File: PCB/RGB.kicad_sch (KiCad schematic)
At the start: 70 parts, among them J9 RGB_EX

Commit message: Added large caps to output of TPS2557. Updated STEP file and file data.
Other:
- company: (none) -> Created by Ariamelon (https://github.com/Ariamelon/Honeydew/)
- title: Honeydew unsplit ergonomic keyboard -> Honeydew unified split ergonomic keyboard
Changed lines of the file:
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@@
   (paper "A4")
   (title_block
-    (title "Honeydew unsplit ergonomic keyboard")
-    (date "2023-04-03")
+    (title "Honeydew unified split ergonomic keyboard")
+    (date "2023-04-08")
     (rev "V2.0")
+    (company "Created by Ariamelon (https://github.com/Ariamelon/Honeydew/)")
     (comment 1 "All capacitors 50V unless otherwise specified.")
+    (comment 2 "Licensed under CC BY 4.0.")
   )
   (junction (at 234.95 60.96) (diameter 0) (color 0 0 0 0)

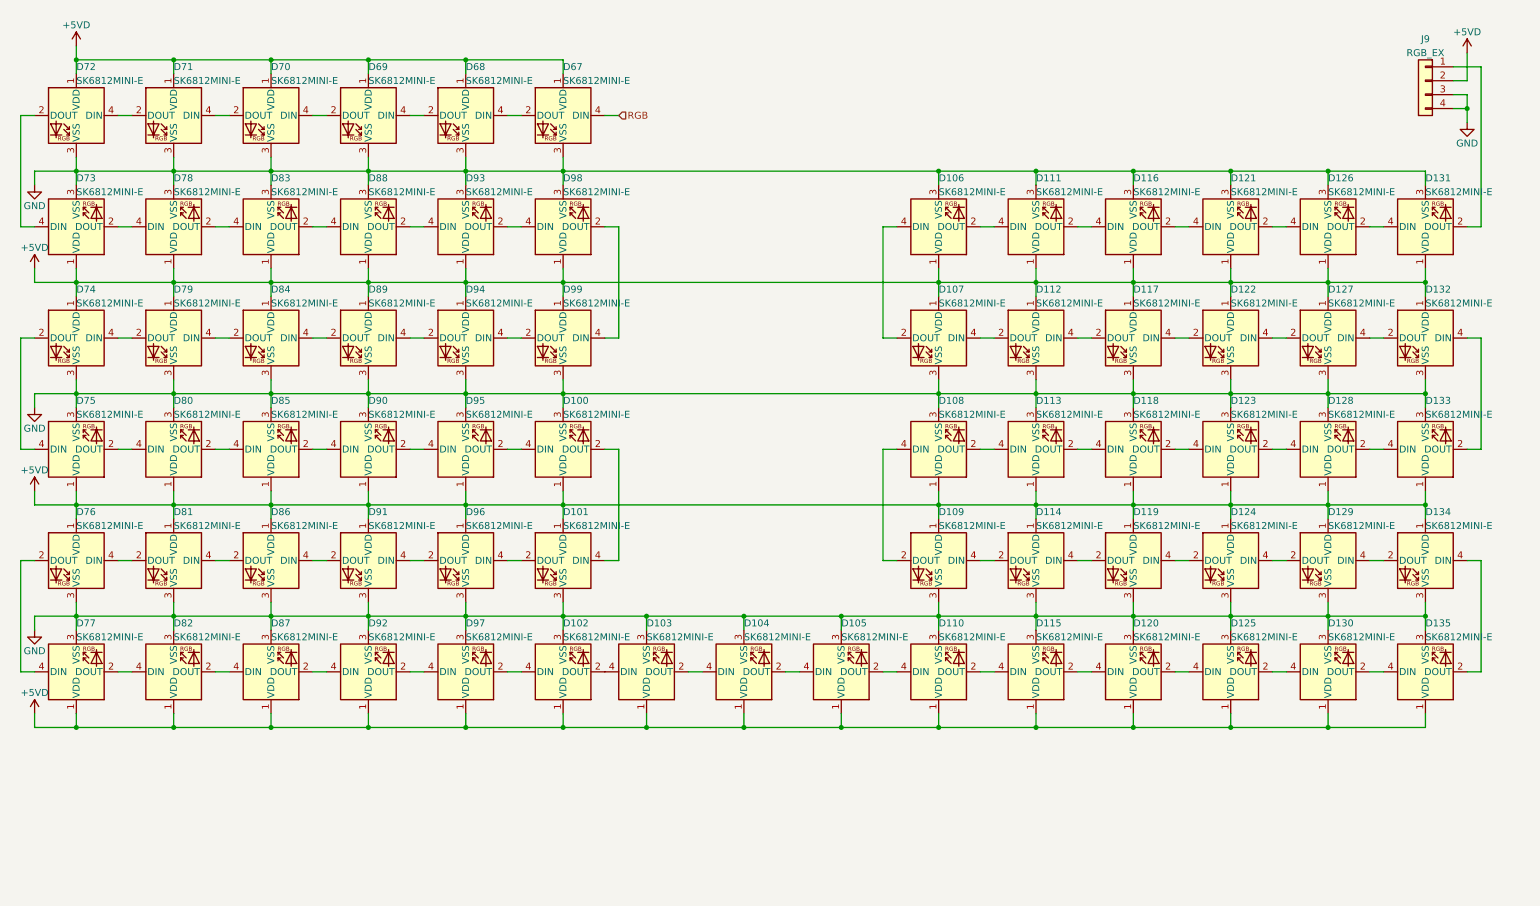
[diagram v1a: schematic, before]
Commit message: Shrunk size of PCB.
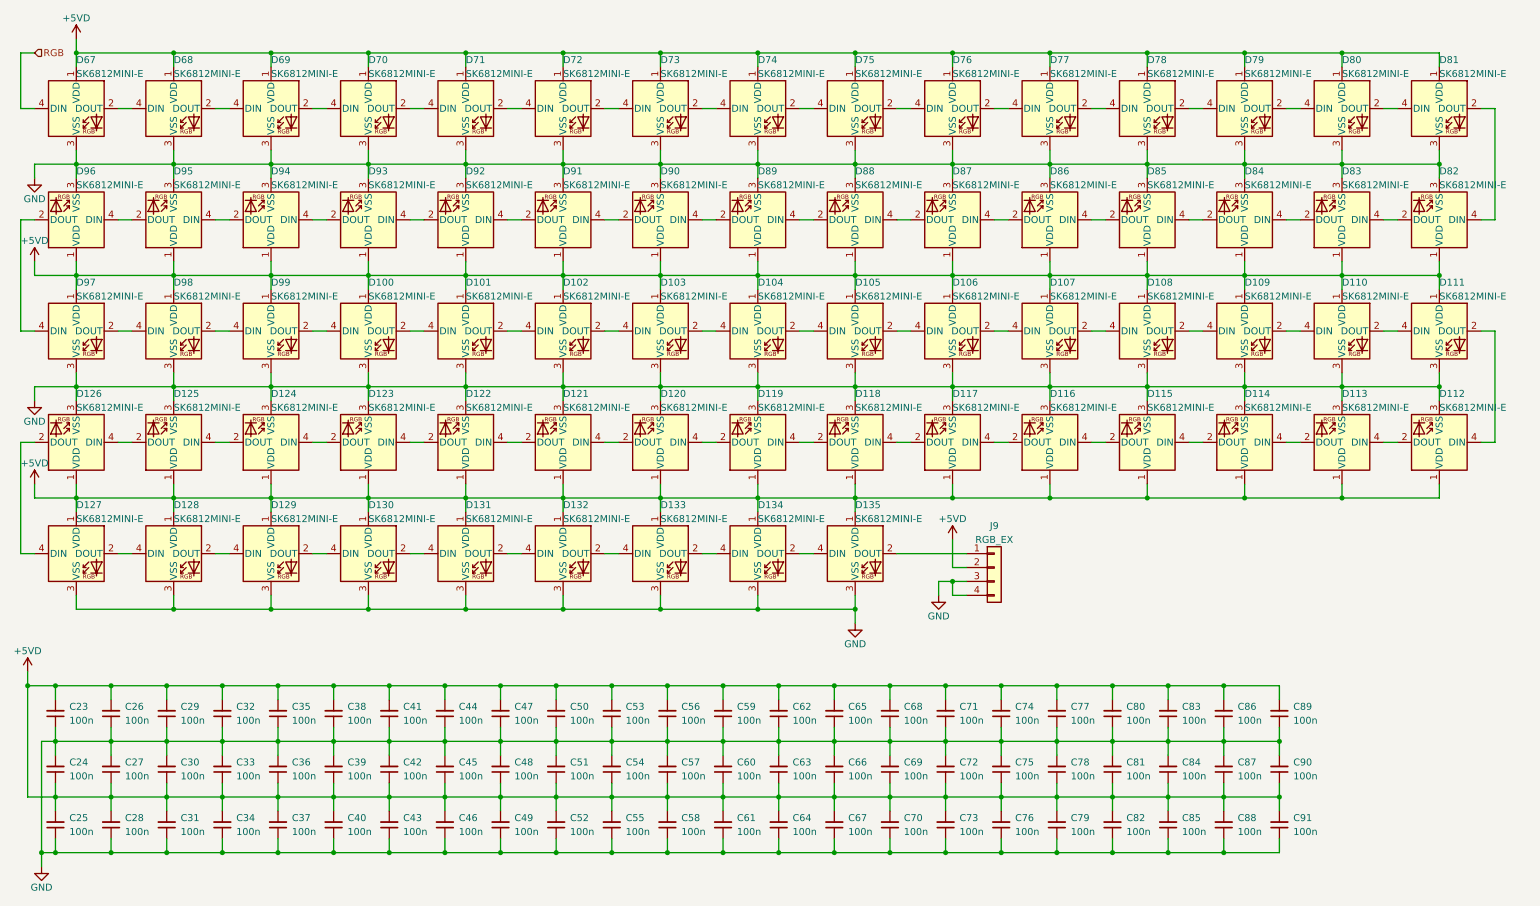
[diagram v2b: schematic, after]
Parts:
- added C23, C24, C25, C26, C27, C28, C29, C30, C31, C32, C33, C34, C35, C36, C37, C38, C39, C40, C41, C42, C43, C44, C45, C46, C47, C48, C49, C50, C51, C52, C53, C54, C55, C56, C57, C58, C59, C60, C61, C62, C63, C64, C65, C66, C67, C68, C69, C70, C71, C72, C73, C74, C75, C76, C77, C78, C79, C80, C81, C82, C83, C84, C85, C86, C87, C88, C89, C90, C91: 100n, Honeydew:C_0402_1005Metric, symbol Device:C_Small
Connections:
- net +5VD: now also C23.2, C24.1, C25.2, C26.2, C27.1, C28.2, C29.2, C30.1, C31.2, C32.2, C33.1, C34.2, C35.2, C36.1, C37.2, C38.2, C39.1, C40.2, C41.2, C42.1, C43.2, C44.2, C45.1, C46.2, C47.2, C48.1, C49.2, C50.2, C51.1, C52.2, C53.2, C54.1, C55.2, C56.2, C57.1, C58.2, C59.2, C60.1, C61.2, C62.2, C63.1, C64.2, C65.2, C66.1, C67.2, C68.2, C69.1, C70.2, C71.2, C72.1, C73.2, C74.2, C75.1, C76.2, C77.2, C78.1, C79.2, C80.2, C81.1, C82.2, C83.2, C84.1, C85.2, C86.2, C87.1, C88.2, C89.2, C90.1, C91.2
- net GND: now also C23.1, C24.2, C25.1, C26.1, C27.2, C28.1, C29.1, C30.2, C31.1, C32.1, C33.2, C34.1, C35.1, C36.2, C37.1, C38.1, C39.2, C40.1, C41.1, C42.2, C43.1, C44.1, C45.2, C46.1, C47.1, C48.2, C49.1, C50.1, C51.2, C52.1, C53.1, C54.2, C55.1, C56.1, C57.2, C58.1, C59.1, C60.2, C61.1, C62.1, C63.2, C64.1, C65.1, C66.2, C67.1, C68.1, C69.2, C70.1, C71.1, C72.2, C73.1, C74.1, C75.2, C76.1, C77.1, C78.2, C79.1, C80.1, C81.2, C82.1, C83.1, C84.2, C85.1, C86.1, C87.2, C88.1, C89.1, C90.2, C91.1
- net at D89.4 (DIN): now also D88.2 (DOUT); no longer D94.2 (DOUT)
- net at D94.4 (DIN): now also D93.2 (DOUT); no longer D99.2 (DOUT)
- net at D110.2 (DOUT): now also D111.4 (DIN); no longer D115.4 (DIN)
- net at D105.2 (DOUT): now also D106.4 (DIN); no longer D110.4 (DIN)
- net at D132.4 (DIN): now also D131.2 (DOUT); no longer D133.2 (DOUT)
- net at D128.2 (DOUT): now also D129.4 (DIN); no longer D133.4 (DIN)
- net at D74.4 (DIN): now also D73.2 (DOUT); no longer D79.2 (DOUT)
- net at D79.4 (DIN): now also D78.2 (DOUT); no longer D84.2 (DOUT)
- net at D89.2 (DOUT): now also D90.4 (DIN); no longer D84.4 (DIN)
- net at D107.2 (DOUT): now also D108.4 (DIN); no longer D106.4 (DIN)
- net at D107.4 (DIN): now also D106.2 (DOUT); no longer D112.2 (DOUT)
- net at D81.2 (DOUT): now also D82.4 (DIN); no longer D76.4 (DIN)
- net at D86.2 (DOUT): now also D87.4 (DIN); no longer D81.4 (DIN)
- net at D130.2 (DOUT): now also D131.4 (DIN); no longer D135.4 (DIN)
- net at D125.2 (DOUT): now also D126.4 (DIN); no longer D130.4 (DIN)
- net at D83.4 (DIN): now also D82.2 (DOUT); no longer D78.2 (DOUT)
- net at D78.4 (DIN): now also D77.2 (DOUT); no longer D73.2 (DOUT)
- net at D88.4 (DIN): now also D87.2 (DOUT); no longer D83.2 (DOUT)
- net at D98.4 (DIN): now also D97.2 (DOUT); no longer D93.2 (DOUT)
- net at D92.2 (DOUT): now also D93.4 (DIN); no longer D97.4 (DIN)
- net at D92.4 (DIN): now also D91.2 (DOUT); no longer D87.2 (DOUT)
- net at D111.2 (DOUT): now also D112.4 (DIN); no longer D116.4 (DIN)
- net at D115.2 (DOUT): now also D116.4 (DIN); no longer D120.4 (DIN)
- net at D125.4 (DIN): now also D124.2 (DOUT); no longer D120.2 (DOUT)
- net at D126.2 (DOUT): now also D127.4 (DIN); no longer D131.4 (DIN)
- net at D121.2 (DOUT): now also D122.4 (DIN); no longer D126.4 (DIN)
- net at D102.4 (DIN): now also D101.2 (DOUT); no longer D97.2 (DOUT)
- net at D86.4 (DIN): now also D85.2 (DOUT); no longer D91.2 (DOUT)
- net at D116.2 (DOUT): now also D117.4 (DIN); no longer D121.4 (DIN)
- net at D100.4 (DIN): now also D99.2 (DOUT); no longer D95.2 (DOUT)
- net at D127.2 (DOUT): now also D128.4 (DIN); no longer D122.4 (DIN)
- net at D132.2 (DOUT): now also D133.4 (DIN); no longer D127.4 (DIN)
- net at D109.2 (DOUT): now also D110.4 (DIN); no longer D108.4 (DIN)
- net at D114.2 (DOUT): now also D115.4 (DIN); no longer D109.4 (DIN)
- net at D95.4 (DIN): now also D94.2 (DOUT); no longer D90.2 (DOUT)
- net at D108.2 (DOUT): now also D109.4 (DIN); no longer D113.4 (DIN)
- net at D134.2 (DOUT): now also D135.4 (DIN); no longer D129.4 (DIN)
- net at D135.2 (DOUT): now also J9.1 (Pin_1); no longer D134.4 (DIN)
- net at D123.2 (DOUT): now also D124.4 (DIN); no longer D128.4 (DIN)
- net at D123.4 (DIN): now also D122.2 (DOUT); no longer D118.2 (DOUT)
- net at D117.2 (DOUT): now also D118.4 (DIN); no longer D112.4 (DIN)
- net at D75.2 (DOUT): now also D76.4 (DIN); no longer D80.4 (DIN)
- net at D114.4 (DIN): now also D113.2 (DOUT); no longer D119.2 (DOUT)
- net at D91.4 (DIN): now also D90.2 (DOUT); no longer D96.2 (DOUT)
- net at D96.4 (DIN): now also D95.2 (DOUT); no longer D101.2 (DOUT)
- net at D80.2 (DOUT): now also D81.4 (DIN); no longer D85.4 (DIN)
- net at D129.2 (DOUT): now also D130.4 (DIN); no longer D124.4 (DIN)
- net at D119.4 (DIN): now also D118.2 (DOUT); no longer D124.2 (DOUT)
- new net: D112.2 (DOUT), D113.4 (DIN)
- new net: D120.2 (DOUT), D121.4 (DIN)
- new net: D79.2 (DOUT), D80.4 (DIN)
- new net: D84.2 (DOUT), D85.4 (DIN)
- new net: D119.2 (DOUT), D120.4 (DIN)
- new net: D83.2 (DOUT), D84.4 (DIN)
- new net: D133.2 (DOUT), D134.4 (DIN)
- new net: D96.2 (DOUT), D97.4 (DIN)
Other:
- moved on the sheet: J9

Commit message: 17/04/2023 large update.
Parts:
- removed C23, C24, C25, C26, C27, C28, C29, C30, C31, C32, C33, C34, C35, C36, C37, C38, C39, C40, C41, C42, C43, C44, C45, C46, C47, C48, C49, C50, C51, C52, C53, C54, C55, C56, C57, C58, C59, C60, C61, C62, C63, C64, C65, C66, C67, C68, C69, C70, C71, C72, C73, C74, C75, C76, C77, C78, C79, C80, C81, C82, C83, C84, C85, C86, C87, C88, C89, C90, C91: 100n, Honeydew:C_0402_1005Metric, symbol Device:C_Small
- added C104 (x3), C97: 47u, Capacitor_SMD:C_1206_3216Metric, symbol Device:C_Small
- added D136, D137, D138: SK6812MINI-E, Honeydew:YS-SK6812MINI-E, symbol Honeydew:SK6812MINI-E
- J9: footprint Honeydew:PinHeader_1x04_P2.54mm_Vertical_SIlkless -> Honeydew:Header_RGB
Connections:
- net GND: now also C104.1, C104.1, C104.1, C97.1, D136.3 (VSS), D137.3 (VSS), D138.3 (VSS)
- net at D135.2 (DOUT): now also D136.4 (DIN); no longer J9.1 (Pin_1)
- net +5VD renamed +5V
- net +5V: now also C104.2, C104.2, C104.2, C97.2, D136.1 (VDD), D137.1 (VDD), D138.1 (VDD)
- new net: D136.2 (DOUT), D137.4 (DIN)
- new net: D137.2 (DOUT), D138.4 (DIN)
- new net: D138.2 (DOUT), J9.1 (Pin_1)
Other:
- moved on the sheet: D100, D101, D102, D103, D104, D105, D106, D107, D108, D109, D110, D111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

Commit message: Rerouting.
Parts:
- removed C104 (x3), C97: 47u, Capacitor_SMD:C_1206_3216Metric, symbol Device:C_Small
- added C31, C32: 100u, Capacitor_Tantalum_SMD:CP_EIA-6032-15_Kemet-U, symbol Device:C_Polarized_Small
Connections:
- net +5V: now also C31.1, C32.1
- net GND: now also C31.2, C32.2
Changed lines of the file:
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@@
   (junction (at 130.81 41.91) (diameter 0) (color 0 0 0 0)
   )
-  (junction (at 33.02 135.89) (diameter 0) (color 0 0 0 0)
-  )
   (junction (at 95.25 102.87) (diameter 0) (color 0 0 0 0)
   )
@@
   (junction (at 166.37 102.87) (diameter 0) (color 0 0 0 0)
   )
-  (junction (at 33.02 146.05) (diameter 0) (color 0 0 0 0)
-  )
   (junction (at 95.25 21.59) (diameter 0) (color 0 0 0 0)
   )
@@
   (junction (at 41.91 123.19) (diameter 0) (color 0 0 0 0)
   )
-  (junction (at 41.91 146.05) (diameter 0) (color 0 0 0 0)
-  )
   (junction (at 255.27 102.87) (diameter 0) (color 0 0 0 0)
   )
-  (junction (at 41.91 135.89) (diameter 0) (color 0 0 0 0)
-  )
   (junction (at 130.81 123.19) (diameter 0) (color 0 0 0 0)
   )
@@
     (stroke (width 0) (type default))
   )
-  (wire (pts (xy 41.91 146.05) (xy 41.91 143.51))
-    (stroke (width 0) (type default))
-  )
   (wire (pts (xy 237.49 110.49) (xy 237.49 115.57))
     (stroke (width 0) (type default))
@@
     (stroke (width 0) (type default))
   )
-  (wire (pts (xy 41.91 135.89) (xy 50.8 135.89))
-    (stroke (width 0) (type default))
-  )
   (wire (pts (xy 130.81 85.09) (xy 130.81 82.55))
     (stroke (width 0) (type default))
@@
     (stroke (width 0) (type default))
   )
-  (wire (pts (xy 33.02 146.05) (xy 41.91 146.05))
-    (stroke (width 0) (type default))
-  )
   (wire (pts (xy 201.93 59.69) (xy 201.93 62.23))
     (stroke (width 0) (type default))
@@
     (stroke (width 0) (type default))
   )
-  (wire (pts (xy 41.91 135.89) (xy 41.91 138.43))
-    (stroke (width 0) (type default))
-  )
   (wire (pts (xy 255.27 100.33) (xy 255.27 102.87))
     (stroke (width 0) (type default))
@@
     (stroke (width 0) (type default))
   )
-  (wire (pts (xy 33.02 135.89) (xy 41.91 135.89))
-    (stroke (width 0) (type default))
-  )
   (wire (pts (xy 130.81 21.59) (xy 130.81 24.13))
     (stroke (width 0) (type default))
@@
     (stroke (width 0) (type default))
   )
-  (wire (pts (xy 50.8 135.89) (xy 50.8 138.43))
-    (stroke (width 0) (type default))
-  )
   (wire (pts (xy 148.59 44.45) (xy 148.59 41.91))
     (stroke (width 0) (type default))
@@
     (stroke (width 0) (type default))
   )
-  (wire (pts (xy 41.91 146.05) (xy 50.8 146.05))
-    (stroke (width 0) (type default))
-  )
   (wire (pts (xy 166.37 120.65) (xy 166.37 123.19))
     (stroke (width 0) (type default))
@@
     (stroke (width 0) (type default))
   )
-  (wire (pts (xy 50.8 146.05) (xy 50.8 143.51))
-    (stroke (width 0) (type default))
-  )
   (wire (pts (xy 41.91 102.87) (xy 24.13 102.87))
     (stroke (width 0) (type default))
@@
     )
   )
-  (symbol (lib_id "Device:C_Small") (at 50.8 140.97 180) (unit 1)
-    (in_bom yes) (on_board yes) (dnp no)
-    (property "Reference" "C104" (at 53.34 138.43 0)
-      (effects (font (size 1.27 1.27)) (justify right))
-    )
-    (property "Value" "47u" (at 53.34 140.97 0)
-      (effects (font (size 1.27 1.27)) (justify right))
-    )
-    (property "Footprint" "Capacitor_SMD:C_1206_3216Metric" (at 50.8 140.97 0)
-      (effects (font (size 1.27 1.27)) hide)
-    )
-    (property "Datasheet" "" (at 50.8 140.97 0)
-      (effects (font (size 1.27 1.27)) hide)
-    )
-    (property "Description" "1206 capacitor" (at 50.8 140.97 0)
-      (effects (font (size 1.27 1.27)) hide)
-    )
-    (property "LCSC" "C96123" (at 50.8 140.97 0)
-      (effects (font (size 1.27 1.27)) hide)
-    )
-    (property "Voltage" "10V" (at 53.34 143.51 0)
-      (effects (font (size 1.27 1.27)) (justify right))
-    )
-    (pin "1")
-    (pin "2")
-    (instances
-      (project "Honeydew"
-        (path "/534caec7-cf60-4f90-b1ed-42c9d445ef0f/0e23afb1-1d24-49d7-b6b4-dea31b732359"
-          (reference "C104") (unit 1)
-        )
-        (path "/534caec7-cf60-4f90-b1ed-42c9d445ef0f/6e258a66-57df-44a5-ad7a-a7c1b9255fcb"
-          (reference "C34") (unit 1)
-        )
-      )
-    )
-  )
   (symbol (lib_name "SK6812MINI-E_54") (lib_id "Honeydew:SK6812MINI-E") (at 113.03 31.75 0) (unit 1)
     (in_bom yes) (on_board yes) (dnp no)
@@
     )
   )
-  (symbol (lib_id "Device:C_Small") (at 24.13 140.97 180) (unit 1)
-    (in_bom yes) (on_board yes) (dnp no)
-    (property "Reference" "C97" (at 26.67 138.43 0)
-      (effects (font (size 1.27 1.27)) (justify right))
-    )
-    (property "Value" "47u" (at 26.67 140.97 0)
-      (effects (font (size 1.27 1.27)) (justify right))
-    )
-    (property "Footprint" "Capacitor_SMD:C_1206_3216Metric" (at 24.13 140.97 0)
-      (effects (font (size 1.27 1.27)) hide)
-    )
-    (property "Datasheet" "" (at 24.13 140.97 0)
-      (effects (font (size 1.27 1.27)) hide)
-    )
-    (property "Description" "1206 capacitor" (at 24.13 140.97 0)
-      (effects (font (size 1.27 1.27)) hide)
-    )
-    (property "LCSC" "C96123" (at 24.13 140.97 0)
-      (effects (font (size 1.27 1.27)) hide)
-    )
-    (property "Voltage" "10V" (at 26.67 143.51 0)
-      (effects (font (size 1.27 1.27)) (justify right))
-    )
-    (pin "1")
-    (pin "2")
-    (instances
-      (project "Honeydew"
-        (path "/534caec7-cf60-4f90-b1ed-42c9d445ef0f/0e23afb1-1d24-49d7-b6b4-dea31b732359"
-          (reference "C97") (unit 1)
-        )
-        (path "/534caec7-cf60-4f90-b1ed-42c9d445ef0f/6e258a66-57df-44a5-ad7a-a7c1b9255fcb"
-          (reference "C31") (unit 1)
-        )
-      )
-    )
-  )
   (symbol (lib_name "SK6812MINI-E_54") (lib_id "Honeydew:SK6812MINI-E") (at 273.05 72.39 0) (unit 1)
     (in_bom yes) (on_board yes) (dnp no)
@@
     )
   )
-  (symbol (lib_id "Device:C_Small") (at 33.02 140.97 180) (unit 1)
-    (in_bom yes) (on_board yes) (dnp no)
-    (property "Reference" "C104" (at 35.56 138.43 0)
-      (effects (font (size 1.27 1.27)) (justify right))
+  (symbol (lib_id "Device:C_Polarized_Small") (at 33.02 140.97 0) (unit 1)
+    (in_bom yes) (on_board yes) (dnp no) (fields_autoplaced)
+    (property "Reference" "C32" (at 35.56 139.7889 0)
+      (effects (font (size 1.27 1.27)) (justify left))
     )
-    (property "Value" "47u" (at 35.56 140.97 0)
-      (effects (font (size 1.27 1.27)) (justify right))
+    (property "Value" "100u" (at 35.56 142.3289 0)
+      (effects (font (size 1.27 1.27)) (justify left))
     )
-    (property "Footprint" "Capacitor_SMD:C_1206_3216Metric" (at 33.02 140.97 0)
+    (property "Footprint" "Capacitor_Tantalum_SMD:CP_EIA-6032-15_Kemet-U" (at 33.02 140.97 0)
       (effects (font (size 1.27 1.27)) hide)
     )
-    (property "Datasheet" "" (at 33.02 140.97 0)
+    (property "Datasheet" "~" (at 33.02 140.97 0)
       (effects (font (size 1.27 1.27)) hide)
     )
-    (property "Description" "1206 capacitor" (at 33.02 140.97 0)
+    (property "Description" "6032 Tantalum" (at 33.02 140.97 0)
       (effects (font (size 1.27 1.27)) hide)
     )
-    (property "LCSC" "C96123" (at 33.02 140.97 0)
+    (property "LCSC" "C273664" (at 33.02 140.97 0)
       (effects (font (size 1.27 1.27)) hide)
     )
-    (property "Voltage" "10V" (at 35.56 143.51 0)
-      (effects (font (size 1.27 1.27)) (justify right))
-    )
     (pin "1")
     (pin "2")
     (instances
       (project "Honeydew"
-        (path "/534caec7-cf60-4f90-b1ed-42c9d445ef0f/0e23afb1-1d24-49d7-b6b4-dea31b732359"
-          (reference "C104") (unit 1)
-        )
         (path "/534caec7-cf60-4f90-b1ed-42c9d445ef0f/6e258a66-57df-44a5-ad7a-a7c1b9255fcb"
           (reference "C32") (unit 1)
@@
     )
   )
-  (symbol (lib_id "Device:C_Small") (at 41.91 140.97 180) (unit 1)
-    (in_bom yes) (on_board yes) (dnp no)
-    (property "Reference" "C104" (at 44.45 138.43 0)
-      (effects (font (size 1.27 1.27)) (justify right))
-    )
-    (property "Value" "47u" (at 44.45 140.97 0)
-      (effects (font (size 1.27 1.27)) (justify right))
-    )
-    (property "Footprint" "Capacitor_SMD:C_1206_3216Metric" (at 41.91 140.97 0)
-      (effects (font (size 1.27 1.27)) hide)
-    )
-    (property "Datasheet" "" (at 41.91 140.97 0)
-      (effects (font (size 1.27 1.27)) hide)
-    )
-    (property "Description" "1206 capacitor" (at 41.91 140.97 0)
-      (effects (font (size 1.27 1.27)) hide)
-    )
-    (property "LCSC" "C96123" (at 41.91 140.97 0)
-      (effects (font (size 1.27 1.27)) hide)
-    )
-    (property "Voltage" "10V" (at 44.45 143.51 0)
-      (effects (font (size 1.27 1.27)) (justify right))
-    )
-    (pin "1")
-    (pin "2")
-    (instances
-      (project "Honeydew"
-        (path "/534caec7-cf60-4f90-b1ed-42c9d445ef0f/0e23afb1-1d24-49d7-b6b4-dea31b732359"
-          (reference "C104") (unit 1)
-        )
-        (path "/534caec7-cf60-4f90-b1ed-42c9d445ef0f/6e258a66-57df-44a5-ad7a-a7c1b9255fcb"
-          (reference "C33") (unit 1)
-        )
-      )
-    )
-  )
   (symbol (lib_name "SK6812MINI-E_54") (lib_id "Honeydew:SK6812MINI-E") (at 255.27 72.39 0) (unit 1)
     (in_bom yes) (on_board yes) (dnp no)
@@
         )
       )
+    )
+  )
+  (symbol (lib_id "Device:C_Polarized_Small") (at 24.13 140.97 0) (unit 1)
+    (in_bom yes) (on_board yes) (dnp no) (fields_autoplaced)
+    (property "Reference" "C31" (at 26.67 139.7889 0)
+      (effects (font (size 1.27 1.27)) (justify left))
+    )
+    (property "Value" "100u" (at 26.67 142.3289 0)
+      (effects (font (size 1.27 1.27)) (justify left))
+    )
+    (property "Footprint" "Capacitor_Tantalum_SMD:CP_EIA-6032-15_Kemet-U" (at 24.13 140.97 0)
+      (effects (font (size 1.27 1.27)) hide)
+    )
+    (property "Datasheet" "~" (at 24.13 140.97 0)
+      (effects (font (size 1.27 1.27)) hide)
+    )
+    (property "Description" "6032 Tantalum" (at 24.13 140.97 0)
+      (effects (font (size 1.27 1.27)) hide)
+    )
+    (property "LCSC" "C273664" (at 24.13 140.97 0)
+      (effects (font (size 1.27 1.27)) hide)
+    )
+    (pin "1")
+    (pin "2")
+    (instances
+      (project "Honeydew"
+        (path "/534caec7-cf60-4f90-b1ed-42c9d445ef0f/6e258a66-57df-44a5-ad7a-a7c1b9255fcb"
+          (reference "C31") (unit 1)
+        )
+      )
